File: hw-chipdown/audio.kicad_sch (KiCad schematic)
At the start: 12 parts, among them U10 PCM5100

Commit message: Almost final PicoGUS 2.0
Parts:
- C21, C22: footprint Capacitor_SMD:C_0402_1005Metric -> Capacitor_SMD:C_0603_1608Metric
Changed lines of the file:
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@@
       (effects (font (size 1.27 1.27)))
     )
-    (property "Footprint" "Capacitor_SMD:C_0402_1005Metric" (at 90.805 50.8 0)
+    (property "Footprint" "Capacitor_SMD:C_0603_1608Metric" (at 90.805 50.8 0)
       (effects (font (size 1.27 1.27)) hide)
     )
@@
       (effects (font (size 1.27 1.27)))
     )
-    (property "Footprint" "Capacitor_SMD:C_0402_1005Metric" (at 90.805 43.18 0)
+    (property "Footprint" "Capacitor_SMD:C_0603_1608Metric" (at 90.805 43.18 0)
       (effects (font (size 1.27 1.27)) hide)
     )

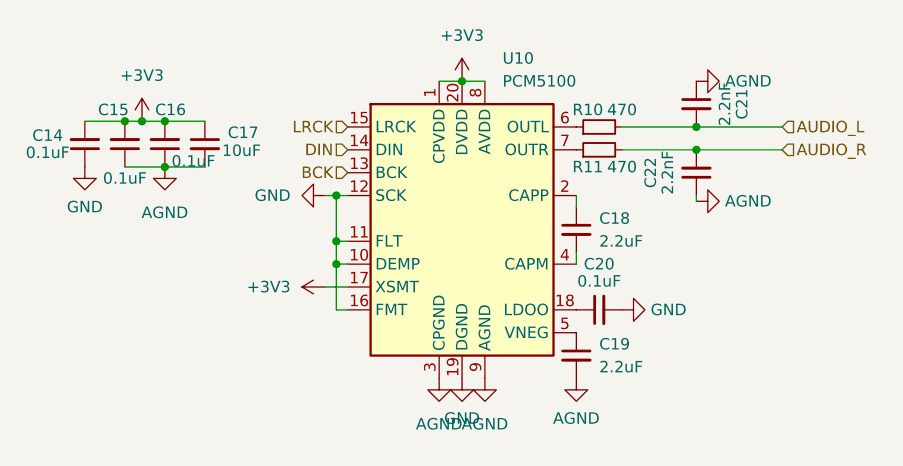
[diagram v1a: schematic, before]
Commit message: PicoGUS v2.0 produced at JLCPCB 2023-10-23
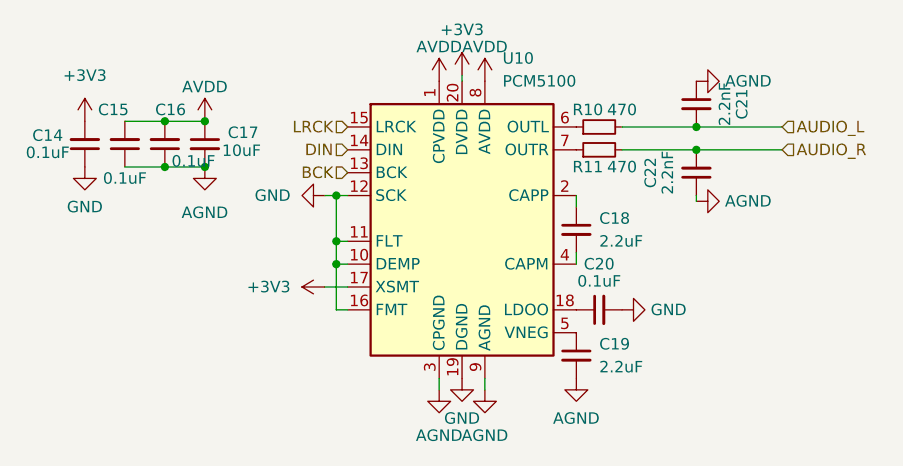
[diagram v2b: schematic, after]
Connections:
- net +3V3: no longer C15.2, C16.2, C17.1, U10.1 (CPVDD), U10.8 (AVDD)
- net GNDS renamed AGND
- new net AVDD: C15.2, C16.2, C17.1, U10.1 (CPVDD), U10.8 (AVDD)
